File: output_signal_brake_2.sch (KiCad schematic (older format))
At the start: 28 parts, among them P1 CONN_6_RA_MALE, P2 CONN_6_RA_FEMALE, P3 CONN_6_RA_MALE, P4 CONN_6_RA_MALE, P5 CONN_6_MALE_FRONT, P6 CONN_6_MALE_BACK, U39 TLC59108IPWR, U40 TLC59108IPWR, U41 TLC59108IPWR, U42 TPS62090

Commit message: replacement of parts, moved parts, preparing for routing
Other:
- note added: "-30%< L <+20%"
- note added: "-50% < C < +20%"
- note added: "1.4MHz operation"
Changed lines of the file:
@@
 Sheet 9 16
 Title ""
-Date "1 feb 2014"
+Date "3 feb 2014"
 Rev ""
 Comp ""
@@
 Wire Wire Line
 	9000 4650 8950 4650
+Text Notes 8450 6150 0    60   ~ 0
+1.4MHz operation
+Text Notes 8400 5100 0    60   ~ 0
+-30%< L <+20%
+Text Notes 9450 5150 0    60   ~ 0
+-50% < C < +20%
 $EndSCHEMATC

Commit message: revised connections between boards
now right and left will be identical and easy to assemble.
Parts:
- removed P2: CONN_6_RA_FEMALE, symbol CONN_6
- removed P3, P4: CONN_6_RA_MALE, symbol CONN_6
- removed P6: CONN_6_MALE_BACK, symbol CONN_6
- added P2, P3: CONN_2x2_MALE_RA, symbol CONN_4
- added P4, P6: CONN_2x2_FEMALE_BACK, symbol CONN_4
- P5: value CONN_6_MALE_FRONT -> CONN_6_FEMALE_FRONT
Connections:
- wire segments 183 -> 173

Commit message: routed the back light module
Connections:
- wire segments 173 -> 170
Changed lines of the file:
@@
 Sheet 9 16
 Title ""
-Date "13 feb 2014"
+Date "16 feb 2014"
 Rev ""
 Comp ""
@@
 L +3.3V #PWR080
 U 1 1 52EDDB8A
-P 10300 4100
-F 0 "#PWR080" H 10300 4060 30  0001 C CNN
-F 1 "+3.3V" H 10300 4210 30  0000 C CNN
-F 2 "" H 10300 4100 60  0000 C CNN
-F 3 "" H 10300 4100 60  0000 C CNN
-	1    10300 4100
+P 9700 4250
+F 0 "#PWR080" H 9700 4210 30  0001 C CNN
+F 1 "+3.3V" H 9700 4360 30  0000 C CNN
+F 2 "" H 9700 4250 60  0000 C CNN
+F 3 "" H 9700 4250 60  0000 C CNN
+	1    9700 4250
 	-1   0    0    -1
 $EndComp
@@
 	-1   0    0    -1
 $EndComp
-Text Label 10300 4300 2    60   ~ 0
+Text Label 10300 4450 2    60   ~ 0
 +2.5V local
 Text HLabel 10300 4800 0    60   BiDi ~ 0
@@
 Text HLabel 10300 4700 0    60   Input ~ 0
 SCL
-Text HLabel 10300 4450 0    60   Input ~ 0
+Text HLabel 10300 4350 0    60   Input ~ 0
 ~RESET
 $Comp
@@
 L +3.3V #PWR082
 U 1 1 52EDF40B
-P 8950 4200
-F 0 "#PWR082" H 8950 4160 30  0001 C CNN
-F 1 "+3.3V" H 8950 4310 30  0000 C CNN
-F 2 "" H 8950 4200 60  0000 C CNN
-F 3 "" H 8950 4200 60  0000 C CNN
-	1    8950 4200
+P 8300 4350
+F 0 "#PWR082" H 8300 4310 30  0001 C CNN
+F 1 "+3.3V" H 8300 4460 30  0000 C CNN
+F 2 "" H 8300 4350 60  0000 C CNN
+F 3 "" H 8300 4350 60  0000 C CNN
+	1    8300 4350
 	-1   0    0    -1
 $EndComp
@@
 	-1   0    0    -1
 $EndComp
-Text Label 8950 4350 2    60   ~ 0
+Text Label 8950 4250 2    60   ~ 0
 +2.5V local
 Text HLabel 8950 4550 0    60   BiDi ~ 0
@@
 	5800 3550 5700 3650
 Wire Wire Line
-	10300 4100 10300 4150
-Wire Wire Line
 	10300 4150 10350 4150
 Wire Wire Line
@@
 	10300 4900 10300 4950
 Wire Wire Line
-	10350 4300 10300 4300
-Wire Wire Line
 	10350 4700 10300 4700
 Wire Wire Line
@@
 	10350 4450 10300 4450
 Wire Wire Line
-	8950 4200 8950 4250
-Wire Wire Line
 	8950 4250 9000 4250
 Wire Wire Line
@@
 	8950 4750 8950 4800
 Wire Wire Line
-	9000 4350 8950 4350
+	8300 4350 9000 4350
 Wire Wire Line
 	9000 4450 8950 4450
@@
 	10000 4600 10000 4900
 Connection ~ 10300 4900
-Wire Wire Line
-	10350 4250 10350 4350
-Connection ~ 10350 4300
+Text Label 10300 4150 2    60   ~ 0
++2.5V local
+Wire Wire Line
+	10300 4350 10350 4350
+Wire Wire Line
+	9700 4250 10350 4250
 $Comp
 L +3.3V #PWR084
-U 1 1 52F71619
-P 10650 1950
-F 0 "#PWR084" H 10650 1910 30  0001 C CNN
-F 1 "+3.3V" H 10650 2060 30  0000 C CNN
-F 2 "" H 10650 1950 60  0000 C CNN
-F 3 "" H 10650 1950 60  0000 C CNN
-	1    10650 1950
+U 1 1 530021E7
+P 10700 2100
+F 0 "#PWR084" H 10700 2060 30  0001 C CNN
+F 1 "+3.3V" H 10700 2210 30  0000 C CNN
+F 2 "" H 10700 2100 60  0000 C CNN
+F 3 "" H 10700 2100 60  0000 C CNN
+	1    10700 2100
 	1    0    0    -1
 $EndComp
 $Comp
 L DGND #PWR085
-U 1 1 52F7161F
+U 1 1 530021ED
 P 10650 2800
 F 0 "#PWR085" H 10650 2800 40  0001 C CNN
@@
 	1    0    0    -1
 $EndComp
-Text Label 10650 2150 0    60   ~ 0
+Text Label 10650 2300 0    60   ~ 0
 +2.5V local
 Text HLabel 10650 2650 2    60   BiDi ~ 0
@@
 Text HLabel 10650 2550 2    60   Input ~ 0
 SCL
-Text HLabel 10650 2300 2    60   Input ~ 0
+Text HLabel 10650 2200 2    60   Input ~ 0
 ~RESET
 Wire Wire Line
-	10650 1950 10650 2000
-Wire Wire Line
 	10650 2000 10600 2000
 Wire Wire Line
-	10950 2750 10600 2750
+	10600 2750 10950 2750
 Wire Wire Line
 	10650 2750 10650 2800
-Wire Wire Line
-	10600 2150 10650 2150
 Wire Wire Line
 	10600 2550 10650 2550
@@
 	10950 2450 10950 2750
 Connection ~ 10650 2750
-Wire Wire Line
-	10600 2100 10600 2200
-Connection ~ 10600 2150
+Text Label 10650 2000 0    60   ~ 0
++2.5V local
+Wire Wire Line
+	10650 2200 10600 2200
+Wire Wire Line
+	10700 2100 10600 2100
 $EndSCHEMATC

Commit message: finished routing board, added vibrator module
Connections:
- net labels added: +2.5V
- wire segments 170 -> 171
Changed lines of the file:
@@
 Sheet 9 16
 Title ""
-Date "16 feb 2014"
+Date "17 feb 2014"
 Rev ""
 Comp ""
@@
 SDA
 $Comp
-L DGND #PWR052
+L DGND #PWR045
 U 1 1 52A16DFC
 P 7500 3500
-F 0 "#PWR052" H 7500 3500 40  0001 C CNN
+F 0 "#PWR045" H 7500 3500 40  0001 C CNN
 F 1 "DGND" H 7500 3430 40  0000 C CNN
 F 2 "" H 7500 3500 60  0000 C CNN
@@
 $EndComp
 $Comp
-L DGND #PWR053
+L DGND #PWR046
 U 1 1 52A16E02
 P 1450 3600
-F 0 "#PWR053" H 1450 3600 40  0001 C CNN
+F 0 "#PWR046" H 1450 3600 40  0001 C CNN
 F 1 "DGND" H 1450 3530 40  0000 C CNN
 F 2 "" H 1450 3600 60  0000 C CNN
@@
 $EndComp
 $Comp
-L +3.3V #PWR054
+L +3.3V #PWR047
 U 1 1 52A17165
 P 7500 2550
-F 0 "#PWR054" H 7500 2510 30  0001 C CNN
+F 0 "#PWR047" H 7500 2510 30  0001 C CNN
 F 1 "+3.3V" H 7500 2660 30  0000 C CNN
 F 2 "" H 7500 2550 60  0000 C CNN
@@
 $EndComp
 $Comp
-L +3.3V #PWR055
+L +3.3V #PWR048
 U 1 1 52A171EB
 P 1450 2650
-F 0 "#PWR055" H 1450 2610 30  0001 C CNN
+F 0 "#PWR048" H 1450 2610 30  0001 C CNN
 F 1 "+3.3V" H 1450 2760 30  0000 C CNN
 F 2 "" H 1450 2650 60  0000 C CNN
@@
 $EndComp
 $Comp
-L DGND #PWR056
+L DGND #PWR049
 U 1 1 52A1749B
 P 10250 3500
-F 0 "#PWR056" H 10250 3500 40  0001 C CNN
+F 0 "#PWR049" H 10250 3500 40  0001 C CNN
 F 1 "DGND" H 10250 3430 40  0000 C CNN
 F 2 "" H 10250 3500 60  0000 C CNN
@@
 $EndComp
 $Comp
-L DGND #PWR057
+L DGND #PWR050
 U 1 1 52A174A9
 P 4200 3600
-F 0 "#PWR057" H 4200 3600 40  0001 C CNN
+F 0 "#PWR050" H 4200 3600 40  0001 C CNN
 F 1 "DGND" H 4200 3530 40  0000 C CNN
 F 2 "" H 4200 3600 60  0000 C CNN
@@
 70mA
 $Comp
-L +3.3V #PWR058
+L +3.3V #PWR051
 U 1 1 52A17BB2
 P 3700 2900
-F 0 "#PWR058" H 3700 2860 30  0001 C CNN
+F 0 "#PWR051" H 3700 2860 30  0001 C CNN
 F 1 "+3.3V" H 3700 3010 30  0000 C CNN
 F 2 "" H 3700 2900 60  0000 C CNN
@@
 $EndComp
 $Comp
-L +3.3V #PWR059
+L +3.3V #PWR052
 U 1 1 52A18346
 P 9750 2800
-F 0 "#PWR059" H 9750 2760 30  0001 C CNN
+F 0 "#PWR052" H 9750 2760 30  0001 C CNN
 F 1 "+3.3V" H 9750 2910 30  0000 C CNN
 F 2 "" H 9750 2800 60  0000 C CNN
@@
 Slave Address\n1000-011x
 $Comp
-L +3.3V #PWR060
+L +3.3V #PWR053
 U 1 1 52A187A3
 P 3450 1550
-F 0 "#PWR060" H 3450 1510 30  0001 C CNN
+F 0 "#PWR053" H 3450 1510 30  0001 C CNN
 F 1 "+3.3V" H 3450 1660 30  0000 C CNN
 F 2 "" H 3450 1550 60  0000 C CNN
@@
 $EndComp
 $Comp
-L DGND #PWR061
+L DGND #PWR054
 U 1 1 52A187A9
 P 3450 2050
-F 0 "#PWR061" H 3450 2050 40  0001 C CNN
+F 0 "#PWR054" H 3450 2050 40  0001 C CNN
 F 1 "DGND" H 3450 1980 40  0000 C CNN
 F 2 "" H 3450 2050 60  0000 C CNN
@@
 $EndComp
 $Comp
-L +3.3V #PWR062
+L +3.3V #PWR055
 U 1 1 52A189EA
 P 9600 1500
-F 0 "#PWR062" H 9600 1460 30  0001 C CNN
+F 0 "#PWR055" H 9600 1460 30  0001 C CNN
 F 1 "+3.3V" H 9600 1610 30  0000 C CNN
 F 2 "" H 9600 1500 60  0000 C CNN
@@
 $EndComp
 $Comp
-L DGND #PWR063
+L DGND #PWR056
 U 1 1 52A189F0
 P 9600 2000
-F 0 "#PWR063" H 9600 2000 40  0001 C CNN
+F 0 "#PWR056" H 9600 2000 40  0001 C CNN
 F 1 "DGND" H 9600 1930 40  0000 C CNN
 F 2 "" H 9600 2000 60  0000 C CNN
@@
 BATT_IN
 $Comp
-L DGND #PWR064
+L DGND #PWR057
 U 1 1 52A7FDF9
 P 6400 5550
-F 0 "#PWR064" H 6400 5550 40  0001 C CNN
+F 0 "#PWR057" H 6400 5550 40  0001 C CNN
 F 1 "DGND" H 6400 5480 40  0000 C CNN
 F 2 "" H 6400 5550 60  0000 C CNN
@@
 $EndComp
 $Comp
-L DGND #PWR065
+L DGND #PWR058
 U 1 1 52A7FDFF
 P 6500 6300
-F 0 "#PWR065" H 6500 6300 40  0001 C CNN
+F 0 "#PWR058" H 6500 6300 40  0001 C CNN
 F 1 "DGND" H 6500 6230 40  0000 C CNN
 F 2 "" H 6500 6300 60  0000 C CNN
@@
 $EndComp
 $Comp
-L DGND #PWR066
+L DGND #PWR059
 U 1 1 52A7FE05
 P 7500 6700
-F 0 "#PWR066" H 7500 6700 40  0001 C CNN
+F 0 "#PWR059" H 7500 6700 40  0001 C CNN
 F 1 "DGND" H 7500 6630 40  0000 C CNN
 F 2 "" H 7500 6700 60  0000 C CNN
@@
 $EndComp
 $Comp
-L DGND #PWR067
+L DGND #PWR060
 U 1 1 52A7FE0B
 P 9400 5900
-F 0 "#PWR067" H 9400 5900 40  0001 C CNN
+F 0 "#PWR060" H 9400 5900 40  0001 C CNN
 F 1 "DGND" H 9400 5830 40  0000 C CNN
 F 2 "" H 9400 5900 60  0000 C CNN
@@
 $EndComp
 $Comp
-L DGND #PWR068
+L DGND #PWR061
 U 1 1 52A7FE11
 P 9900 5550
-F 0 "#PWR068" H 9900 5550 40  0001 C CNN
+F 0 "#PWR061" H 9900 5550 40  0001 C CNN
 F 1 "DGND" H 9900 5480 40  0000 C CNN
 F 2 "" H 9900 5550 60  0000 C CNN
@@
 ~RESET
 $Comp
-L +3.3V #PWR069
+L +3.3V #PWR062
 U 1 1 52B1B0D0
 P 5750 6700
-F 0 "#PWR069" H 5750 6660 30  0001 C CNN
+F 0 "#PWR062" H 5750 6660 30  0001 C CNN
 F 1 "+3.3V" H 5750 6810 30  0000 C CNN
 F 2 "" H 5750 6700 60  0000 C CNN
@@
 $EndComp
 $Comp
-L DGND #PWR070
+L DGND #PWR063
 U 1 1 52B1BF30
 P 6050 7250
-F 0 "#PWR070" H 6050 7250 40  0001 C CNN
+F 0 "#PWR063" H 6050 7250 40  0001 C CNN
 F 1 "DGND" H 6050 7180 40  0000 C CNN
 F 2 "" H 6050 7250 60  0000 C CNN
@@
 $EndComp
 $Comp
-L DGND #PWR071
+L DGND #PWR064
 U 1 1 52B2FFCD
 P 10150 6250
-F 0 "#PWR071" H 10150 6250 40  0001 C CNN
+F 0 "#PWR064" H 10150 6250 40  0001 C CNN
 F 1 "DGND" H 10150 6180 40  0000 C CNN
 F 2 "" H 10150 6250 60  0000 C CNN
@@
 $EndSheet
 $Comp
-L DGND #PWR072
+L DGND #PWR065
 U 1 1 52A189DC
 P 3500 5400
-F 0 "#PWR072" H 3500 5400 40  0001 C CNN
+F 0 "#PWR065" H 3500 5400 40  0001 C CNN
 F 1 "DGND" H 3500 5330 40  0000 C CNN
 F 2 "" H 3500 5400 60  0000 C CNN
@@
 $EndComp
 $Comp
-L +3.3V #PWR073
+L +3.3V #PWR066
 U 1 1 52A189D6
 P 3500 4900
-F 0 "#PWR073" H 3500 4860 30  0001 C CNN
+F 0 "#PWR066" H 3500 4860 30  0001 C CNN
 F 1 "+3.3V" H 3500 5010 30  0000 C CNN
 F 2 "" H 3500 4900 60  0000 C CNN
@@
 ~RESET
 $Comp
-L +3.3V #PWR074
+L +3.3V #PWR067
 U 1 1 52A17FB4
 P 3700 6250
-F 0 "#PWR074" H 3700 6210 30  0001 C CNN
+F 0 "#PWR067" H 3700 6210 30  0001 C CNN
 F 1 "+3.3V" H 3700 6360 30  0000 C CNN
 F 2 "" H 3700 6250 60  0000 C CNN
@@
 $EndComp
 $Comp
-L DGND #PWR075
+L DGND #PWR068
 U 1 1 52A172F3
 P 4200 6950
-F 0 "#PWR075" H 4200 6950 40  0001 C CNN
+F 0 "#PWR068" H 4200 6950 40  0001 C CNN
 F 1 "DGND" H 4200 6880 40  0000 C CNN
 F 2 "" H 4200 6950 60  0000 C CNN
@@
 $EndComp
 $Comp
-L +3.3V #PWR076
+L +3.3V #PWR069
 U 1 1 52A0C661
 P 1450 6000
-F 0 "#PWR076" H 1450 5960 30  0001 C CNN
+F 0 "#PWR069" H 1450 5960 30  0001 C CNN
 F 1 "+3.3V" H 1450 6110 30  0000 C CNN
 F 2 "" H 1450 6000 60  0000 C CNN
@@
 $EndComp
 $Comp
-L DGND #PWR077
+L DGND #PWR070
 U 1 1 52A0C65B
 P 1450 6950
-F 0 "#PWR077" H 1450 6950 40  0001 C CNN
+F 0 "#PWR070" H 1450 6950 40  0001 C CNN
 F 1 "DGND" H 1450 6880 40  0000 C CNN
 F 2 "" H 1450 6950 60  0000 C CNN
@@
 $EndComp
 $Comp
-L +3.3V #PWR078
+L +3.3V #PWR071
 U 1 1 52ED1469
 P 4600 2100
-F 0 "#PWR078" H 4600 2060 30  0001 C CNN
+F 0 "#PWR071" H 4600 2060 30  0001 C CNN
 F 1 "+3.3V" H 4600 2210 30  0000 C CNN
 F 2 "" H 4600 2100 60  0000 C CNN
@@
 $EndComp
 $Comp
-L DGND #PWR079
+L DGND #PWR072
 U 1 1 52ED146F
 P 4600 2700
-F 0 "#PWR079" H 4600 2700 40  0001 C CNN
+F 0 "#PWR072" H 4600 2700 40  0001 C CNN
 F 1 "DGND" H 4600 2630 40  0000 C CNN
 F 2 "" H 4600 2700 60  0000 C CNN
@@
 ~RESET
 $Comp
-L +3.3V #PWR080
+L +3.3V #PWR073
 U 1 1 52EDDB8A
 P 9700 4250
-F 0 "#PWR080" H 9700 4210 30  0001 C CNN
+F 0 "#PWR073" H 9700 4210 30  0001 C CNN
 F 1 "+3.3V" H 9700 4360 30  0000 C CNN
 F 2 "" H 9700 4250 60  0000 C CNN
@@
 $EndComp
 $Comp
-L DGND #PWR081
+L DGND #PWR074
 U 1 1 52EDDB90
 P 10300 4950
-F 0 "#PWR081" H 10300 4950 40  0001 C CNN
+F 0 "#PWR074" H 10300 4950 40  0001 C CNN
 F 1 "DGND" H 10300 4880 40  0000 C CNN
 F 2 "" H 10300 4950 60  0000 C CNN
@@
 $EndComp
 $Comp
-L +3.3V #PWR082
+L +3.3V #PWR075
 U 1 1 52EDF40B
 P 8300 4350
-F 0 "#PWR082" H 8300 4310 30  0001 C CNN
+F 0 "#PWR075" H 8300 4310 30  0001 C CNN
 F 1 "+3.3V" H 8300 4460 30  0000 C CNN
 F 2 "" H 8300 4350 60  0000 C CNN
@@
 $EndComp
 $Comp
-L DGND #PWR083
+L DGND #PWR076
 U 1 1 52EDF411
 P 8950 4800
-F 0 "#PWR083" H 8950 4800 40  0001 C CNN
+F 0 "#PWR076" H 8950 4800 40  0001 C CNN
 F 1 "DGND" H 8950 4730 40  0000 C CNN
 F 2 "" H 8950 4800 60  0000 C CNN
@@
 	9700 4250 10350 4250
 $Comp
-L +3.3V #PWR084
+L +3.3V #PWR077
 U 1 1 530021E7
 P 10700 2100
-F 0 "#PWR084" H 10700 2060 30  0001 C CNN
+F 0 "#PWR077" H 10700 2060 30  0001 C CNN
 F 1 "+3.3V" H 10700 2210 30  0000 C CNN
 F 2 "" H 10700 2100 60  0000 C CNN
@@
 $EndComp
 $Comp
-L DGND #PWR085
+L DGND #PWR078
 U 1 1 530021ED
 P 10650 2800
-F 0 "#PWR085" H 10650 2800 40  0001 C CNN
+F 0 "#PWR078" H 10650 2800 40  0001 C CNN
 F 1 "DGND" H 10650 2730 40  0000 C CNN
 F 2 "" H 10650 2800 60  0000 C CNN
@@
 Wire Wire Line
 	10700 2100 10600 2100
+$Comp
+L +2.5V #PWR079
+U 1 1 530200B6
+P 9300 5200
+F 0 "#PWR079" H 9300 5150 20  0001 C CNN
+F 1 "+2.5V" H 9300 5300 30  0000 C CNN
+F 2 "" H 9300 5200 60  0000 C CNN
+F 3 "" H 9300 5200 60  0000 C CNN
+	1    9300 5200
+	1    0    0    -1
+$EndComp
+Wire Wire Line
+	9300 5200 9300 5250
+Connection ~ 9300 5250
 $EndSCHEMATC

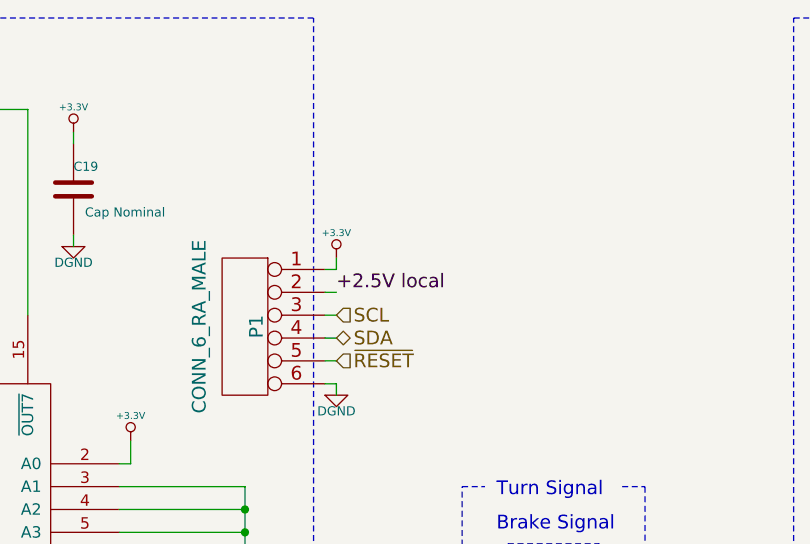
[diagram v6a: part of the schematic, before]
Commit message: revised board for manufacture
still need to panelize
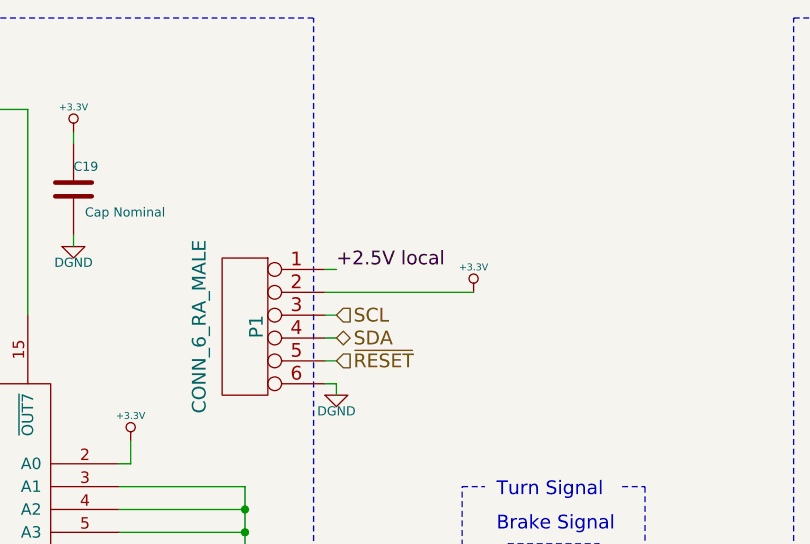
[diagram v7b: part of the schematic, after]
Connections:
- wire segments 171 -> 170
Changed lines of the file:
@@
 Sheet 9 16
 Title ""
-Date "17 feb 2014"
+Date "22 feb 2014"
 Rev ""
 Comp ""
@@
 L +3.3V #PWR071
 U 1 1 52ED1469
-P 4600 2100
-F 0 "#PWR071" H 4600 2060 30  0001 C CNN
-F 1 "+3.3V" H 4600 2210 30  0000 C CNN
-F 2 "" H 4600 2100 60  0000 C CNN
-F 3 "" H 4600 2100 60  0000 C CNN
-	1    4600 2100
+P 5200 2250
+F 0 "#PWR071" H 5200 2210 30  0001 C CNN
+F 1 "+3.3V" H 5200 2360 30  0000 C CNN
+F 2 "" H 5200 2250 60  0000 C CNN
+F 3 "" H 5200 2250 60  0000 C CNN
+	1    5200 2250
 	1    0    0    -1
 $EndComp
@@
 	1    0    0    -1
 $EndComp
-Text Label 4600 2250 0    60   ~ 0
+Text Label 4600 2150 0    60   ~ 0
 +2.5V local
 Text HLabel 4600 2450 2    60   BiDi ~ 0
@@
 	4500 4400 600  4400
 Wire Wire Line
-	4600 2100 4600 2150
-Wire Wire Line
 	4600 2150 4550 2150
 Wire Wire Line
@@
 	4600 2650 4600 2700
 Wire Wire Line
-	4550 2250 4600 2250
+	4550 2250 5200 2250
 Wire Wire Line
 	4550 2350 4600 2350
